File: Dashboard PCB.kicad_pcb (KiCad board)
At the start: 2 copper layers, 150 x 100.2 mm, 66 parts, among them J1 Controls_Leader_Export_02x06, J2 Conn_02x03_CAN, J3 INDICATOR_SWITCH_OUT, J4 FAN_CTRL_01x02, J5 Horn_In_01x02, J6 Horn_Out_01x02, J7 Conn_02x03_CAN, J8 Supp_Out, J9 Supp_In

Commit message: fixed
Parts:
- removed GR_SW: GEAR_SW_12V, switched:3posSlideToggle
- added GEAR_SW: GR_SW1, switched:3posSlideToggle, F.Cu at (120.3, 108.6)
- moved REV_SW 3.34 mm to (115.3, 110.2)
- moved C4 3.29 mm to (128.5, 111.0)
- moved R4 3.29 mm to (125.5, 111.0)
- renumbered BPS_HZD to BPS_HZD1, SUPP_ON to SUPP
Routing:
- net /REV_SW: track 63.6 -> 60.1 mm

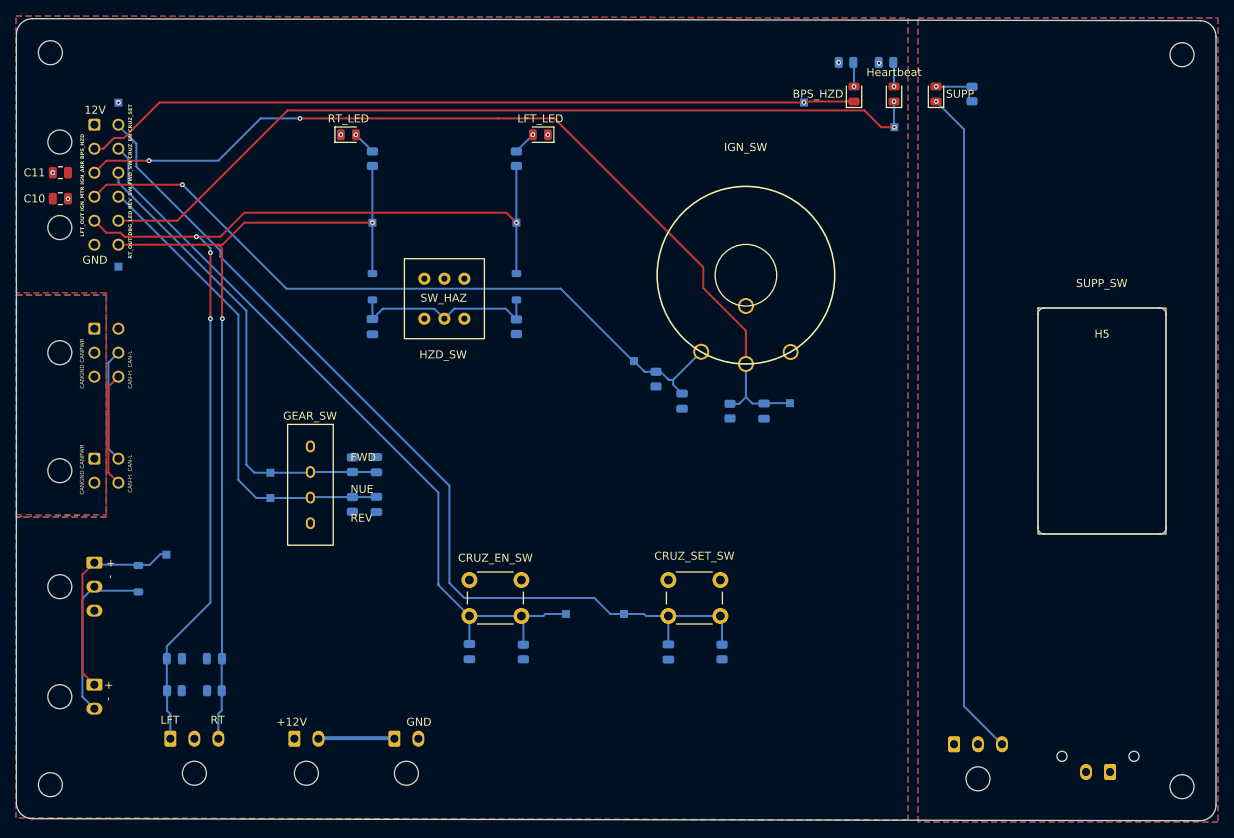
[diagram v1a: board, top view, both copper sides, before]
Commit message: Johnathan
Added FET for horn, fixed other stuff, etc
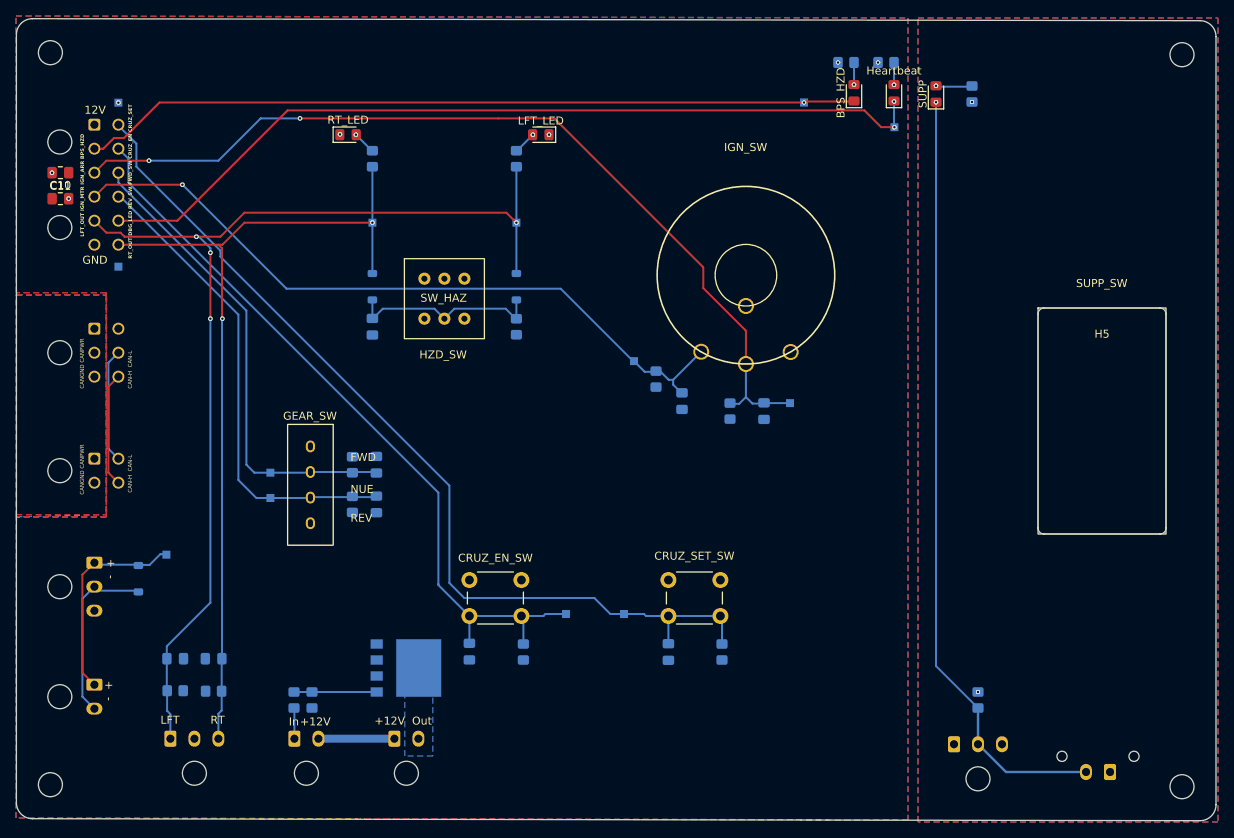
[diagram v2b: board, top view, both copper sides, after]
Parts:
- added Q1: TO200P800X182-5N, Footprints:TO200P800X182-5N, B.Cu at (132.2, 131.5)
- added R15: 10k, Resistor_SMD:R_0805_2012Metric_Pad1.20x1.40mm_HandSolder, B.Cu at (203.8, 135.5)
- added R16: 30k, Resistor_SMD:R_0805_2012Metric_Pad1.20x1.40mm_HandSolder, B.Cu at (118.2, 135.5)
- added R17: 10k, Resistor_SMD:R_0805_2012Metric_Pad1.20x1.40mm_HandSolder, B.Cu at (120.5, 135.5)
- BPS_HZD, Heartbeat, LFT_LED, RT_LED, SUPP: footprint LED_SMD:LED_0805_2012Metric -> LED_SMD:LED_0805_2012Metric_Pad1.15x1.40mm_HandSolder
- C1, C10, C11, C2, C3, C4, C5, C6, C7, C8, C9: footprint Capacitor_SMD:C_0805_2012Metric -> Capacitor_SMD:C_0805_2012Metric_Pad1.18x1.45mm_HandSolder
- R1, R10, R11, R12, R13, R14, R2, R3, R4, R5, R6, R7, R8, R9: footprint Resistor_SMD:R_0805_2012Metric -> Resistor_SMD:R_0805_2012Metric_Pad1.20x1.40mm_HandSolder
- moved BPS_HZD 0.15 mm to (188.2, 59.6)
- moved Heartbeat 0.15 mm to (193.2, 59.6)
- moved R2 0.12 mm to (108.2, 134.4)
- moved C1 0.10 mm to (103.4, 130.3)
- moved R1 0.10 mm to (103.4, 134.3)
- moved C2 0.10 mm to (108.2, 130.3)
- moved LFT_LED 0.05 mm to (149.1, 64.8)
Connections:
- J5 pad 1: +12V -> Net-(J5-Pin_1)
- J5 pad 2: Net-(J5-Pin_2) -> +12V
- J6 pad 1: Net-(J5-Pin_2) -> +12V
- J6 pad 2: GND -> Net-(J6-Pin_2)
- J9 pad 1: /Supp+ -> /Supp-
- R14 pad 1: /LV_EN -> /Supp+
- SUPP pad 1: /Supp- -> /LV_EN
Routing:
- net /LV_EN: track 0.00 -> 97.4 mm, vias 0 -> 1
- net /Supp-: track 83.7 -> 0.00 mm, vias 1 -> 0
- net Net-(Q1-G): track 0.00 -> 10.3 mm
- net +12V: track 0.34 -> 9.84 mm
- net Net-(J5-Pin_2): track 9.50 -> 0.00 mm
- net Net-(J5-Pin_1): track 0.00 -> 3.86 mm
- net /Supp+: vias 0 -> 2
- added copper zone on B.Cu, net /Supp-
- added copper zone on B.Cu, net Net-(J6-Pin_2)
- removed copper zone on B.Cu, net /LV_EN
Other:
- board text added: "In"
- board text added: "Out"

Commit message: pea left pant
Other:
- board text added: "Supp- LV_EN"
- board text removed: "Supp+ LV_EN"
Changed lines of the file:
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@@
 		)
 	)
-	(gr_text "Supp+ LV_EN"
-		(at 223.75 149.75 0)
+	(gr_text "Supp- LV_EN"
+		(at 222.9 149.9 0)
 		(layer "B.SilkS")
 		(effects

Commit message: franK
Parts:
- removed R14: 5.1k, Resistor_SMD:R_0805_2012Metric_Pad1.20x1.40mm_HandSolder
- R15: value 10k -> 5.1k
- renumbered BPS_HZD to BPS, Heartbeat to HBT, Q1 to QD1
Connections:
- J9 pad 1: /Supp- -> /Led
- SUPP pad 1: /LV_EN -> /Led
- SUPP pad 2: Net-(D4-A) -> /Supp-
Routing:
- net /LV_EN: track 97.4 -> 0.00 mm, vias 1 -> 0
- net /Led: track 0.00 -> 92.7 mm, vias 0 -> 1
- net 31: track 0.00 -> 19.5 mm
- net Net-(D4-A): track 5.08 -> 0.00 mm, vias 1 -> 0
- net /Supp-: track 0.00 -> 0.73 mm, vias 0 -> 1
- net /Supp+: vias 2 -> 1
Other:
- board text added: "- LV_EN"
- board text removed: "Supp- LV_EN"

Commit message: frANk
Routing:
- net 31: track 19.5 -> 0.00 mm
- net /LV_EN: track 0.00 -> 19.5 mm
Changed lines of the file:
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@@
 	(net 29 "/Supp-")
 	(net 30 "/Supp+")
+	(net 31 "/LV_EN")
 	(net 32 "Net-(J6-Pin_2)")
 	(net 33 "/Led")

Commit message: Nuked some thigns
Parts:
- removed D3: 1N5819HW, Diode_SMD:D_SOD-123
- removed DASH_FAN1: DASHBOARD_FAN_12V, Connector_Molex:Molex_Micro-Fit_3.0_43650-0300_1x03_P3.00mm_Horizontal
- removed FAN_CTRL: TestPoint, TestPoint:TestPoint_Pad_1.0x1.0mm
- removed J2: Conn_02x03_CAN, Connector_Molex:Molex_Micro-Fit_3.0_43045-0600_2x03_P3.00mm_Horizontal
- removed J4: FAN_CTRL_01x02, Connector_Molex:Molex_Micro-Fit_3.0_43650-0200_1x02_P3.00mm_Horizontal
- removed J7: Conn_02x03_CAN, Connector_Molex:Molex_Micro-Fit_3.0_43045-0400_2x02_P3.00mm_Horizontal
- added 12V: SMD_0805, LED_SMD:LED_0805_2012Metric_Pad1.15x1.40mm_HandSolder, F.Cu at (183.0, 59.5)
- added G***: LHRs_LOGO, Footprints:LHRs_LOGO, B.Cu at (156.5, 109.2)
- added LV_EN: TestPoint, TestPoint:TestPoint_Pad_1.0x1.0mm, B.Cu at (203.8, 132.2)
- added R14: 5.1k, Resistor_SMD:R_0805_2012Metric_Pad1.20x1.40mm_HandSolder, B.Cu at (182.0, 55.8)
- added SUPP+: TestPoint, TestPoint:TestPoint_Pad_1.0x1.0mm, B.Cu at (199.8, 135.2)
- added SUPP-: TestPoint, TestPoint:TestPoint_Pad_1.0x1.0mm, B.Cu at (207.8, 135.2)
- R13: value HZD_RES_VAL -> 5.1k
- moved BPS_HZD 4.57 mm to (186.2, 62.5)
- renumbered BPS_HZD1 to BPS_HZD, QD1 to Q1
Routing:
- net /FAN+: track 26.2 -> 0.00 mm
- net /FAN-: track 22.3 -> 0.00 mm
- net /CAN-L: track 14.3 -> 0.00 mm
- net /CAN-H: track 14.3 -> 0.00 mm
- net +12V: track 9.84 -> 0.34 mm, vias 3 -> 4
- net /LV_EN: track 19.5 -> 24.8 mm
- net Net-(12V_PWR1-A): track 0.00 -> 2.73 mm, vias 0 -> 1
- net /BPS_HZD: track 97.4 -> 98.8 mm
- net GND: vias 4 -> 5
- net /Supp+: vias 1 -> 2
- removed copper zone on F.Cu, net /CAN+12V
- removed copper zone on B.Cu, net /CANGND
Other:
- board text added: "ARRAY"
- board text added: "MOTOR"
- board text added: "OFF"
- board text removed: "+ -"
- board text removed: "CAN"
- board text removed: "CAN-H CAN-L"
- board text removed: "CAN-H CAN-L CANPWR CANGND"
- board text removed: "CANGND CANPWR"
- board text removed: "DASH_FAN"
- board text removed: "Fan Ctrl"
- board text removed: "X"
- board text removed: "X X"

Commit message: Quick change (fuse not added yet)
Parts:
- moved 12V 84.0 mm to (99.0, 57.2)
- moved R14 84.0 mm to (98.0, 53.5)
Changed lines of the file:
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@@
 	(footprint "LED_SMD:LED_0805_2012Metric_Pad1.15x1.40mm_HandSolder"
 		(layer "F.Cu")
-		(at 183 59.5 90)
+		(at 99 57.25 90)
 		(descr "LED SMD 0805 (2012 Metric), square (rectangular) end terminal, IPC_7351 nominal, (Body size source: https://docs.google.com/spreadsheets/d/1BsfQQcO9C6DZCsRaXUlFlo91Tg2WpOkGARC1WS5S8t0/edit?usp=sharing), generated with kicad-footprint-generator")
 		(tags "LED handsolder")
@@
 	(footprint "Resistor_SMD:R_0805_2012Metric_Pad1.20x1.40mm_HandSolder"
 		(layer "B.Cu")
-		(at 182 55.75)
+		(at 98 53.5)
 		(descr "Resistor SMD 0805 (2012 Metric), square (rectangular) end terminal, IPC_7351 nominal with elongated pad for handsoldering. (Body size source: IPC-SM-782 page 72, https://www.pcb-3d.com/wordpress/wp-content/uploads/ipc-sm-782a_amendment_1_and_2.pdf), generated with kicad-footprint-generator")
 		(tags "resistor handsolder")
 		(property "Reference" "R14"
-			(at 0 1.65 360)
+			(at 0 1.65 0)
 			(layer "B.SilkS")
 			(effects
@@
 		)
 		(property "Value" "5.1k"
-			(at 0 -1.65 360)
+			(at 0 -1.65 0)
 			(layer "B.Fab")
 			(effects
@@
 		)
 		(fp_text user "${REFERENCE}"
-			(at 0 0 360)
+			(at 0 0 0)
 			(layer "B.Fab")
 			(effects
@@
 	)
 	(via
-		(at 181 55.75)
+		(at 97 53.5)
 		(size 0.6)
 		(drill 0.3)
@@
 	)
 	(via
-		(at 183 60.525)
+		(at 99 58.275)
 		(size 0.6)
 		(drill 0.3)
@@
 	)
 	(segment
-		(start 183 58.475)
-		(end 183 55.75)
+		(start 99 56.225)
+		(end 99 53.5)
 		(width 0.25)
 		(layer "F.Cu")
@@
 	)
 	(via
-		(at 183 55.75)
+		(at 99 53.5)
 		(size 0.6)
 		(drill 0.3)
@@
 		(polygon
 			(pts
-				(xy 83.5 50) (xy 195 50.25) (xy 195 150.5) (xy 83.5 150.25) (xy 83.548508 112.3375) (xy 83.548508 112.3375)
-				(xy 83.548508 84.5875) (xy 83.548508 84.5875)
+				(xy 83.5 50) (xy 195 50.25) (xy 195 150.5) (xy 83.5 150.25) (xy 83.548508 112.3375) (xy 83.548508 84.5875)
 			)
 		)
@@
 			(pts
 				(xy 83.5 50) (xy 195 50.25) (xy 195 150.5) (xy 83.5 150.25) (xy 83.548508 112.5875) (xy 83.548508 112.3375)
-				(xy 83.548508 84.5875) (xy 83.548508 84.5875)
+				(xy 83.548508 84.5875)
 			)
 		)

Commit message: ravi and lakshay are so mean to me
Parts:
- removed BPS: SMD_0805_RED, LED_SMD:LED_0805_2012Metric_Pad1.15x1.40mm_HandSolder
- removed CRUZ_EN_SW: CRUSE_EN_SW_12V, Button_Switch_THT:SW_PUSH_6mm
- removed CRUZ_SET_SW: CRUSE_SET_SW_12V, Button_Switch_THT:SW_PUSH_6mm
- removed GEAR_SW: GR_SW1, switched:3posSlideToggle
- removed HBT: SMD_0805_GRN, LED_SMD:LED_0805_2012Metric_Pad1.15x1.40mm_HandSolder
- removed HZD_SW: HAZARD_SWITCH_12V, switched:Toggle
- removed LFT_LED, RT_LED: SMD_0805, LED_SMD:LED_0805_2012Metric_Pad1.15x1.40mm_HandSolder
- removed SUPP: LED, LED_SMD:LED_0805_2012Metric_Pad1.15x1.40mm_HandSolder
- added BPS_HZD_LED1: SMD_0805_RED, LED_SMD:LED_0805_2012Metric_Pad1.15x1.40mm_HandSolder, F.Cu at (188.2, 59.6)
- added CRUZ_EN_SW1: CRUSE_EN_SW_12V, Button_Switch_THT:SW_PUSH_6mm, F.Cu at (140.2, 120.5)
- added CRUZ_SET_SW1: CRUSE_SET_SW_12V, Button_Switch_THT:SW_PUSH_6mm, F.Cu at (165.1, 120.5)
- added D3: BZT52-B12-QX, Footprints:BZT52B12QX, B.Cu at (100.2, 55.2)
- added F1: Fuse, Footprints:3588, B.Cu at (113.5, 55.9)
- added GEAR_SW_12V1: GR_SW1, switched:3posSlideToggle, F.Cu at (120.3, 108.6)
- added HZD_SW1: HAZARD_SWITCH_12V, switched:Toggle, F.Cu at (137.1, 85.3)
- added Heartbeat_LED1: SMD_0805_GRN, LED_SMD:LED_0805_2012Metric_Pad1.15x1.40mm_HandSolder, F.Cu at (193.2, 59.6)
- added LFT_LED1: SMD_0805, LED_SMD:LED_0805_2012Metric_Pad1.15x1.40mm_HandSolder, F.Cu at (149.1, 64.9)
- added Q2: Q_PMOS_GDS, Package_TO_SOT_SMD:SOT-23-3, B.Cu at (97.2, 60.2)
- added R18: 100k, Resistor_SMD:R_0805_2012Metric_Pad1.20x1.40mm_HandSolder, B.Cu at (95.2, 55.3)
- added RT_LED1: SMD_0805, LED_SMD:LED_0805_2012Metric_Pad1.15x1.40mm_HandSolder, F.Cu at (125.0, 64.9)
- added SUPP1: LED, LED_SMD:LED_0805_2012Metric_Pad1.15x1.40mm_HandSolder, F.Cu at (198.5, 59.8)
- moved +12V 31.9 mm to (127.0, 52.2)
- moved C10 30.9 mm to (115.6, 57.1), turned to 180 degrees
- moved C11 30.3 mm to (115.6, 54.9)
- moved R14 26.3 mm to (124.2, 53.2), turned to -90 degrees
- moved 12V_PWR1 25.3 mm to (124.2, 57.0)
- renumbered 12V to 12V_PWR1, LV_EN to LV_EN1, SUPP+ to SUPP+1, SUPP- to SUPP-1
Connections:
- J1 pad 1: +12V -> /PWR
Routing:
- net /CRUZ_SET: track 117.2 -> 118.2 mm
- net Net-(12V_PWR1-A): track 2.73 -> 1.73 mm
- net /BPS_HZD: track 98.8 -> 98.7 mm, vias 1 -> 3
- net GND: track 0.00 -> 0.06 mm, vias 5 -> 4
- net /DBG_LED: vias 2 -> 4
- net Net-(LFT_LED1-A): vias 1 -> 2
- net /IGN_ARR: vias 2 -> 4
- added copper zone on B.Cu, net +12V
- added copper zone on B.Cu, net /PWR
- added copper zone on B.Cu, net Net-(D3-A)
- added copper zone on B.Cu, net Net-(D3-K)
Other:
- board text added: "CRUZ_EN"
- board text added: "CRUZ_SET"
- board text added: "Gear"
- board text added: "HBT"
- board text added: "HZD"
- board text added: "Hazard"
- board text added: "SUPP"
